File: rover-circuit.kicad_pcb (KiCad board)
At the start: 2 copper layers, 105 x 70 mm, 46 parts, among them J1 Battery, J3 Recharge Connector, J4 Conn_01x08_Pin, M3 Motor_DC, M4 Motor_DC, M5 Motor_DC, M6 Motor_DC, P1 USB_C_Plug_USB2.0, Q1 AO3401A, SW1 SW_EN, SW2 SW_IO0, SW3 SW_SPDT, U2 ESP32-S3-WROOM-1, U3 TB6612FNG, U4 LM2596S-5, U5 AMS1117-3.3, U7 INA219AxD, U8 TB6612FNG

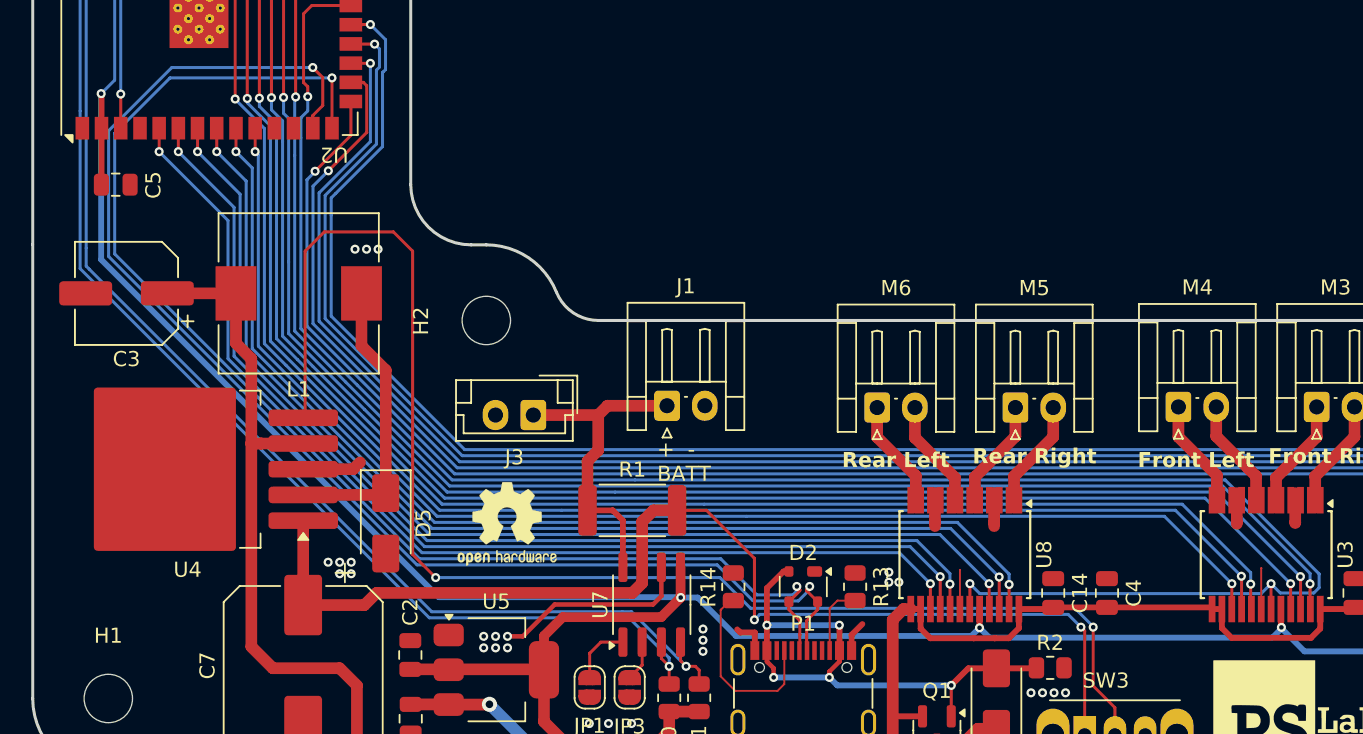
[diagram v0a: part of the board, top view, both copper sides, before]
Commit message: fix: separate standby pins for motor drivers
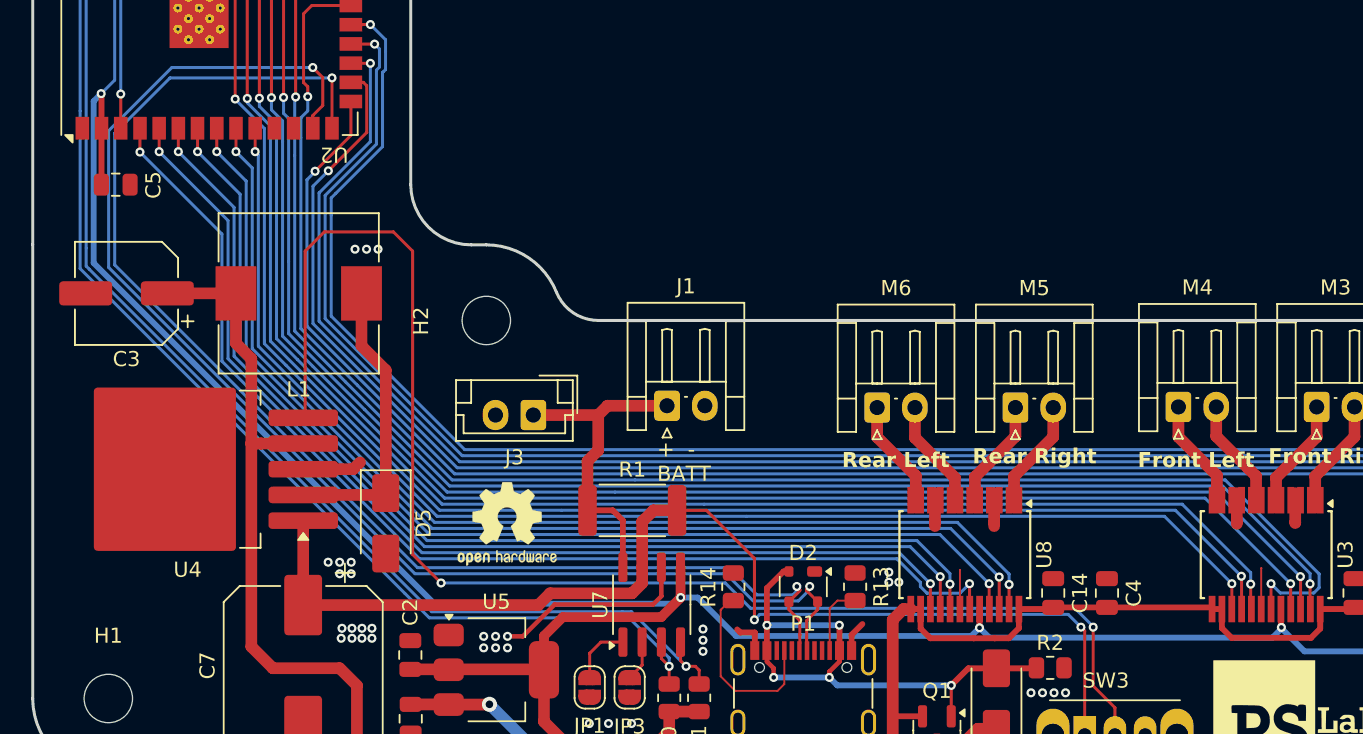
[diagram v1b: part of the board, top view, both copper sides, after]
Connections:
- U2 pad 20: /STBY -> /STBYA
- U2 pad 4: unconnected-(U2-IO4-Pad4) -> /STBYB
- U3 pad 19: /STBY -> /STBYA
- U8 pad 19: /STBY -> /STBYB
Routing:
- net /STBY: track 126.8 -> 0.00 mm, vias 3 -> 0
- net /STBYA: track 0.00 -> 104.7 mm, vias 0 -> 2
- net /STBYB: track 0.00 -> 75.6 mm, vias 0 -> 2
- net +3V3: track 204.0 -> 205.2 mm
- net GND: vias 27 -> 35

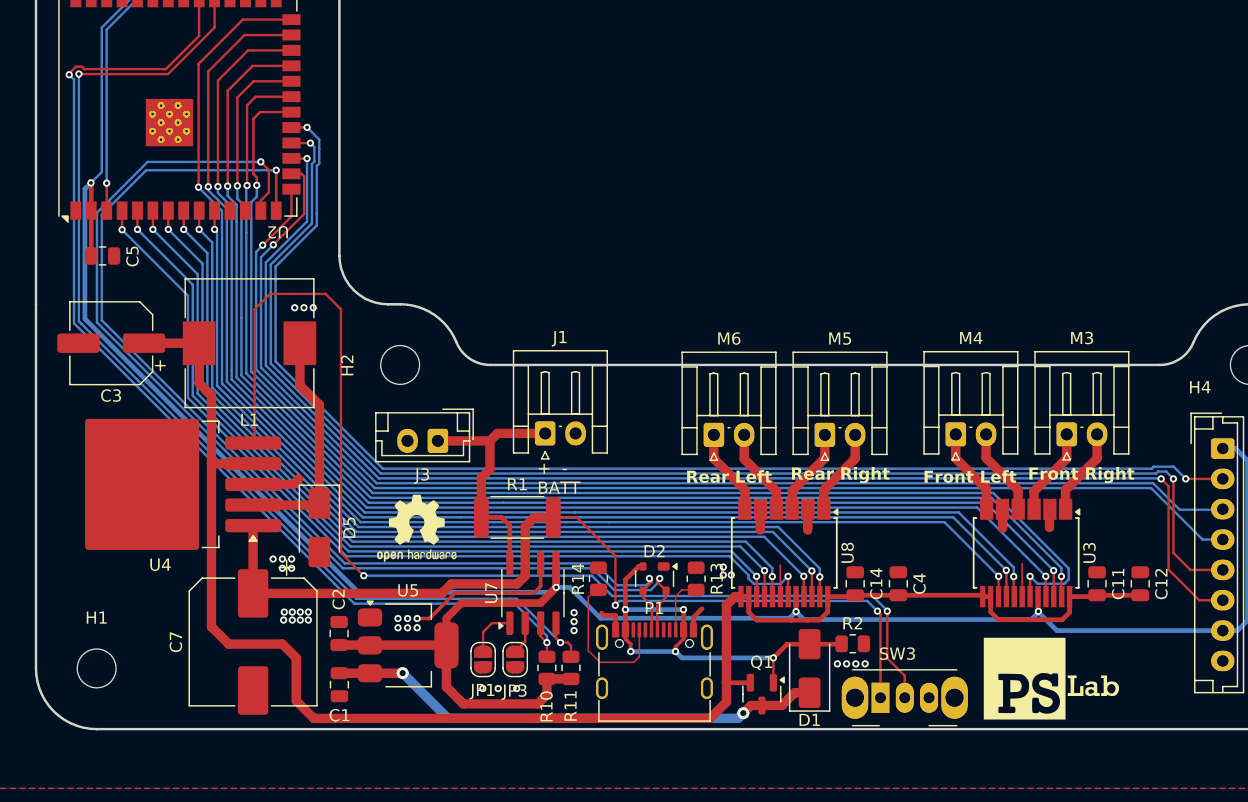
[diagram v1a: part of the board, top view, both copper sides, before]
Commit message: feat: use different 3v3 regulator
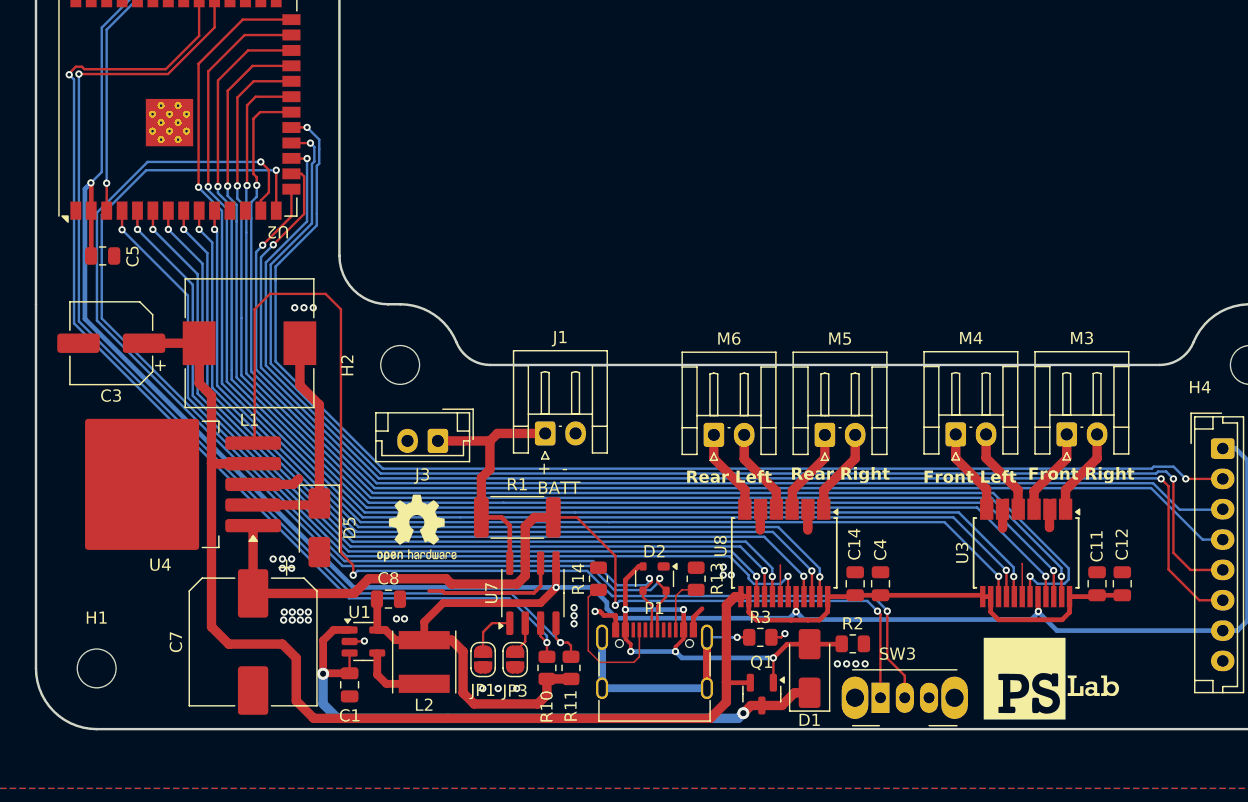
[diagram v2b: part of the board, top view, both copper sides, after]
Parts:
- removed C2: 10uF, Capacitor_SMD:C_0805_2012Metric
- removed U5: AMS1117-3.3, Package_TO_SOT_SMD:SOT-223-3_TabPin2
- added C8: 10uF, Capacitor_SMD:C_0805_2012Metric, F.Cu at (131.9, 123.2)
- added L2: 22uH, Inductor_SMD:L_Taiyo-Yuden_MD-5050, F.Cu at (134.9, 128.4)
- added R3: 0, Resistor_SMD:R_0805_2012Metric, F.Cu at (162.6, 126.3)
- added U1: LM3671MFX-1.25_NOPB, Package_TO_SOT_SMD:SOT-23-5, F.Cu at (129.9, 126.7)
- J4: value Conn_01x08_Pin -> Display Connector
- moved C12 1.48 mm to (192.4, 121.9)
- moved C4 1.47 mm to (172.5, 121.9)
- moved C1 0.84 mm to (128.7, 130.3)
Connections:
- P1 pad S1: GND -> Net-(P1-SHIELD)
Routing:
- net Net-(P1-SHIELD): track 0.00 -> 20.5 mm, vias 0 -> 1
- net Net-(D1-K): track 41.2 -> 53.1 mm
- net Net-(U1-FB): track 0.00 -> 5.98 mm
- net +5V: track 130.6 -> 129.1 mm
- net GND: track 40.1 -> 41.4 mm, vias 35 -> 34
- net +3V3: track 205.2 -> 206.3 mm
- net Net-(SW3-B): track 94.1 -> 94.8 mm

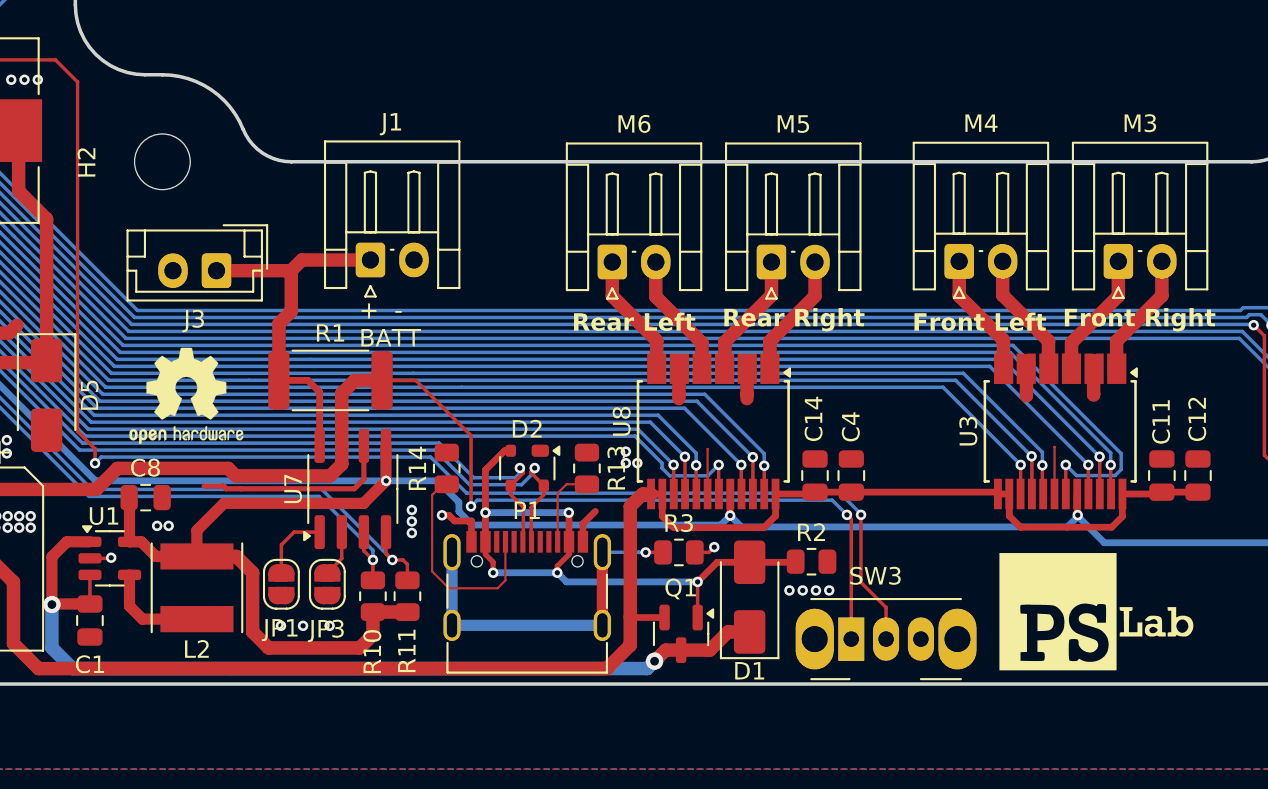
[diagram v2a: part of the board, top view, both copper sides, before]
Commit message: feat: change USB symbol and minor re-routing
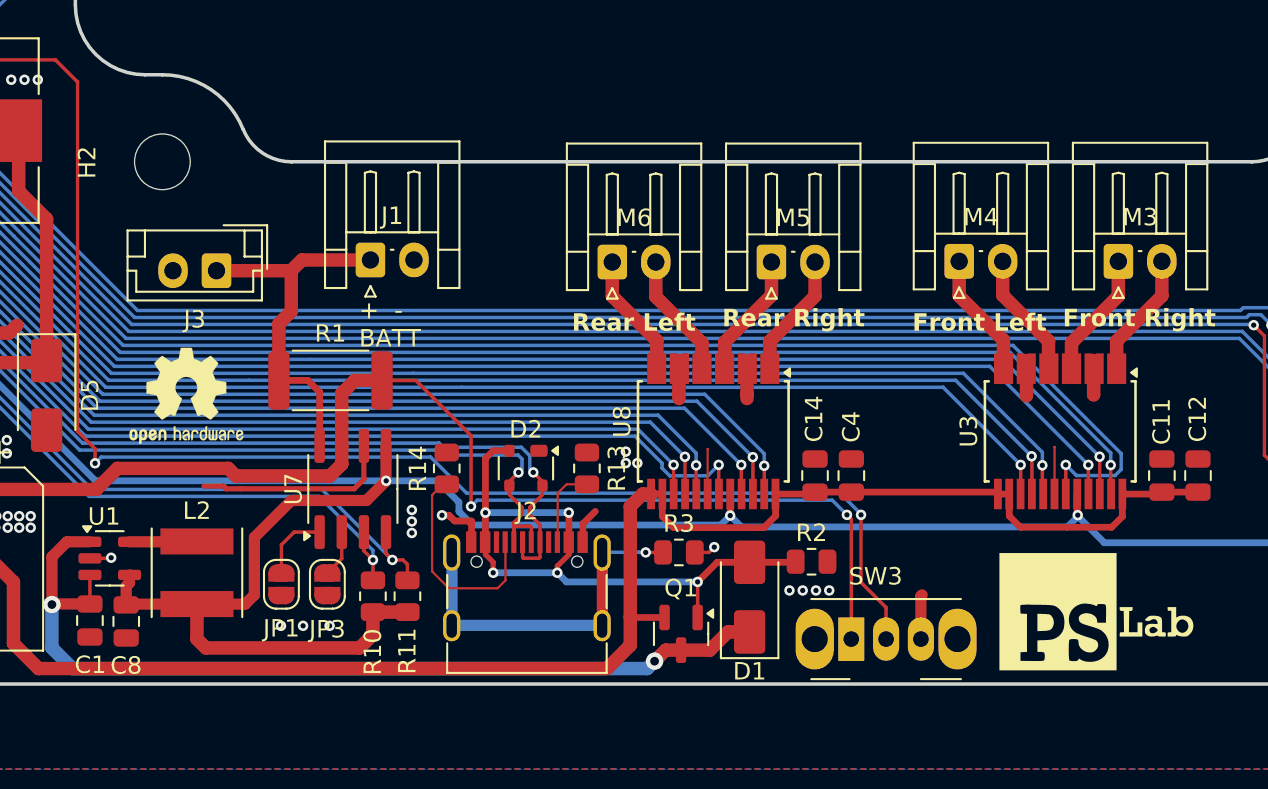
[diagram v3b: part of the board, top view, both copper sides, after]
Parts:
- removed P1: USB_C_Plug_USB2.0, Connector_USB:USB_C_Receptacle_G-Switch_GT-USB-7010ASV
- added J2: USB_C_Receptacle_USB2.0_14P, Connector_USB:USB_C_Receptacle_G-Switch_GT-USB-7010ASV, F.Cu at (153.8, 129.5)
- moved C8 7.20 mm to (130.8, 130.3), turned to -90 degrees
- moved L2 0.86 mm to (134.9, 127.5), turned to -90 degrees
- moved D2 0.08 mm to (153.8, 121.5)
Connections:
- D2 pad 3: /D+ -> /D-
- D2 pad 4: /D- -> /D+
- L2 pad 1: Net-(U1-FB) -> Net-(U1-SW)
- U1 pad 4: Net-(U1-FB) -> +3V3
- U1 pad 5: +3V3 -> Net-(U1-SW)
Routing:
- net Net-(U1-FB): track 5.98 -> 0.00 mm
- net Net-(U1-SW): track 0.00 -> 3.88 mm
- net /D+: track 87.5 -> 90.7 mm
- net GND: track 41.4 -> 44.0 mm, vias 34 -> 32
- net /D-: track 89.7 -> 91.3 mm
- net +3V3: track 206.3 -> 205.6 mm

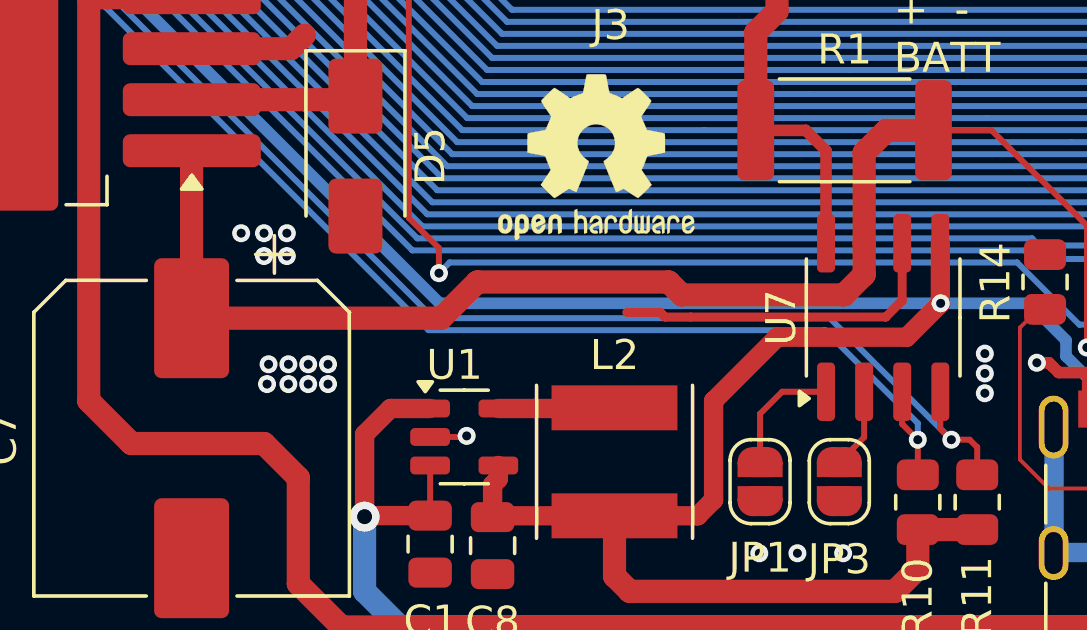
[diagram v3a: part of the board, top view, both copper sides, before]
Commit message: feat: re-route a trace
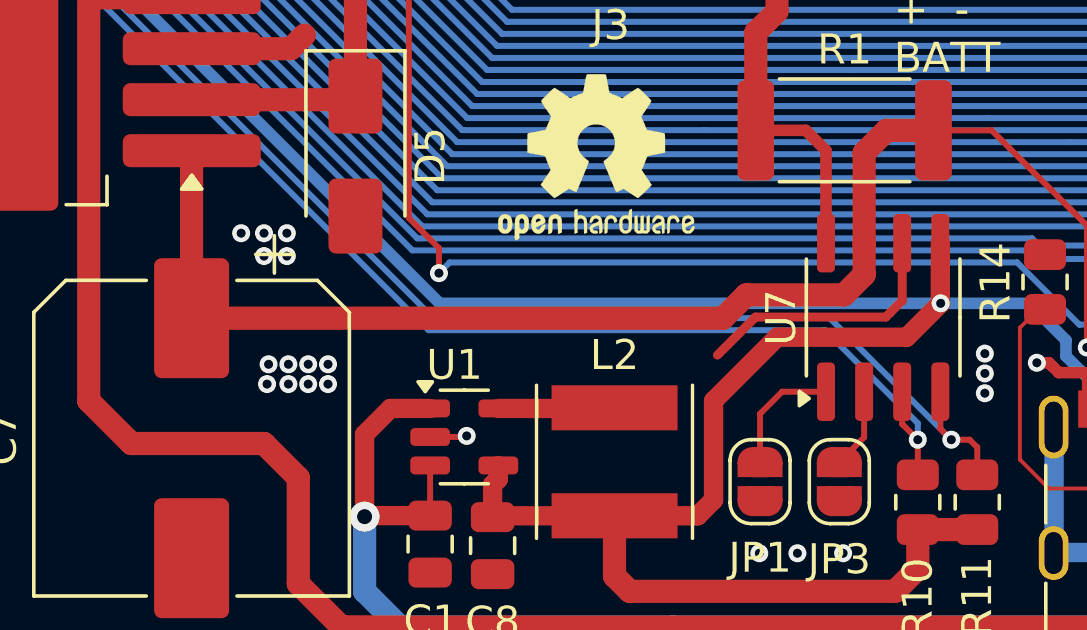
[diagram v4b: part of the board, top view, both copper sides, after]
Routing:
- net GND: track 44.0 -> 41.4 mm
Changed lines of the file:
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@@
 	)
 	(segment
-		(start 144.464 122.1344)
+		(start 144.0492 122.5492)
 		(end 143.9164 122.682)
 		(width 0.3)
@@
 	)
 	(segment
+		(start 139.573 122.682)
+		(end 138.303 123.952)
+		(width 0.3)
+		(layer "F.Cu")
+		(net 1)
+	)
+	(segment
 		(start 150.6458 124.5346)
 		(end 149.6806 124.5346)
@@
 	)
 	(segment
-		(start 136.5504 122.682)
-		(end 136.4488 122.5804)
-		(width 0.3)
-		(layer "F.Cu")
-		(net 1)
-	)
-	(segment
 		(start 157.0458 125.7306)
 		(end 157.0458 124.691)
@@
 	)
 	(segment
+		(start 144.464 122.1344)
+		(end 144.0492 122.5492)
+		(width 0.3)
+		(layer "F.Cu")
+		(net 1)
+	)
+	(segment
 		(start 186.3852 117.248164)
 		(end 186.3852 115.316)
 		(width 0.774192)
-		(layer "F.Cu")
-		(net 1)
-	)
-	(segment
-		(start 136.4488 122.5804)
-		(end 136.398 122.5296)
-		(width 0.3)
-		(layer "F.Cu")
-		(net 1)
-	)
-	(segment
-		(start 136.398 122.5296)
-		(end 135.2804 122.5296)
-		(width 0.3)
 		(layer "F.Cu")
 		(net 1)
@@
 	)
 	(segment
-		(start 137.414 122.682)
-		(end 136.5504 122.682)
-		(width 0.3)
-		(layer "F.Cu")
-		(net 1)
-	)
-	(segment
 		(start 162.56 117.248164)
 		(end 162.56 115.316)
@@
 		(end 166.4716 115.316)
 		(width 0.774192)
-		(layer "F.Cu")
-		(net 1)
-	)
-	(segment
-		(start 143.9164 122.682)
-		(end 137.414 122.682)
-		(width 0.3)
 		(layer "F.Cu")
 		(net 1)
@@
 	)
 	(segment
+		(start 143.9164 122.682)
+		(end 139.573 122.682)
+		(width 0.3)
+		(layer "F.Cu")
+		(net 1)
+	)
+	(segment
 		(start 162.56 117.5004)
 		(end 162.56 117.248164)
@@
 	)
 	(segment
+		(start 142.520896 121.943904)
+		(end 139.26727 121.943904)
+		(width 0.774192)
+		(layer "F.Cu")
+		(net 14)
+	)
+	(segment
 		(start 143.194 120.222)
 		(end 143.194 117.2068)
@@
 	)
 	(segment
-		(start 137.108271 121.943904)
-		(end 136.677967 121.5136)
+		(start 139.26727 121.943904)
+		(end 138.490574 122.7206)
 		(width 0.774192)
 		(layer "F.Cu")
@@
 	)
 	(segment
-		(start 129.095 122.7206)
-		(end 120.777 122.7206)
-		(width 0.774192)
-		(layer "F.Cu")
-		(net 14)
-	)
-	(segment
-		(start 142.520896 121.943904)
-		(end 137.108271 121.943904)
-		(width 0.774192)
-		(layer "F.Cu")
-		(net 14)
-	)
-	(segment
-		(start 136.677967 121.5136)
-		(end 130.302 121.5136)
-		(width 0.774192)
-		(layer "F.Cu")
-		(net 14)
-	)
-	(segment
-		(start 143.194 120.222)
-		(end 143.194 121.2708)
-		(width 0.774192)
-		(layer "F.Cu")
-		(net 14)
-	)
-	(segment
 		(start 172.212 124.1816)
 		(end 172.462 124.4316)
@@
 	)
 	(segment
+		(start 143.194 120.222)
+		(end 143.194 121.2708)
+		(width 0.774192)
+		(layer "F.Cu")
+		(net 14)
+	)
+	(segment
+		(start 120.777 122.7206)
+		(end 120.777 117.1424)
+		(width 0.774192)
+		(layer "F.Cu")
+		(net 14)
+	)
+	(segment
 		(start 143.194 121.2708)
 		(end 142.520896 121.943904)
@@
 	)
 	(segment
-		(start 130.302 121.5136)
-		(end 129.095 122.7206)
-		(width 0.774192)
-		(layer "F.Cu")
-		(net 14)
-	)
-	(segment
-		(start 120.777 122.7206)
-		(end 120.777 117.1424)
-		(width 0.774192)
-		(layer "F.Cu")
+		(start 138.490574 122.7206)
+		(end 120.777 122.7206)
+		(width 0.774192)
+		(layer "F.Cu")

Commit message: finalize components placement
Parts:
- removed REF**: OSHW-Logo2_7.3x6mm_SilkScreen, Symbol:OSHW-Logo2_7.3x6mm_SilkScreen
- added H5: MountingHole, MountingHole:MountingHole_2.5mm, F.Cu at (146.0, 72.7)
- added H6: MountingHole, MountingHole:MountingHole_2.5mm, F.Cu at (204.0, 72.7)
- added H7: MountingHole, MountingHole:MountingHole_2.5mm, F.Cu at (204.0, 95.7)
- added H8: MountingHole, MountingHole:MountingHole_2.5mm, F.Cu at (146.0, 95.7)
- added J5: Raspberry_Pi_2_3, Connector_PinSocket_2.54mm:PinSocket_2x20_P2.54mm_Vertical_SMD, F.Cu at (175.1, 72.8)
- H1, H2, H3, H4: footprint MountingHole:MountingHole_3.2mm_M3 -> MountingHole:MountingHole_3.2mm_M3_Pad
- moved C1 238.0 mm to (-108.4, 109.1)
- moved C12 238.0 mm to (-44.7, 100.7)
- moved C4 238.0 mm to (-64.6, 100.7)
- moved J3 238.0 mm to (-101.1, 89.0)
- moved JP1 238.0 mm to (-97.4, 107.0)
- moved M4 238.0 mm to (-58.4, 88.4)
- moved Q1 238.0 mm to (-74.4, 109.8)
- moved R1 238.0 mm to (-94.5, 95.3)
- moved R10 238.0 mm to (-92.1, 107.7)
- moved R11 238.0 mm to (-90.1, 107.7)
- moved R13 238.0 mm to (-79.8, 100.3)
- moved U7 238.0 mm to (-93.3, 101.5)
- moved C11 238.0 mm to (-46.8, 100.7)
- moved C14 238.0 mm to (-66.7, 100.7)
- moved C3 238.0 mm to (-128.0, 80.9)
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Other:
- board size 105 x 70 mm -> 343.2 x 98.5 mm
